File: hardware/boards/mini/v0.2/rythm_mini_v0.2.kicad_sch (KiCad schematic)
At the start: 76 parts, among them IC1 NAU88C22YG, IC2 IS42S32160F-6BLI, Q1 PMV37EN22, U1 W25Q128JVP, U2 LTV-217-G, U3 RythmMini, U4 STM32H750XBHx, Y1 Crystal_GND24

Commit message: place stm32h750 decoupling capacitors
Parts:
- added C2, C3: 2.2 uF <100 mΩ ESR, Capacitor_SMD:C_0402_1005Metric, symbol Device:C
- added C4: 1uF 600mΩ, Capacitor_SMD:C_0402_1005Metric, symbol Device:C_Small
- added C5: 100nF, Capacitor_SMD:C_0402_1005Metric, symbol Device:C_Small
- added C6: 1uF, Capacitor_SMD:C_0402_1005Metric, symbol Device:C_Small
- added R18: 10k, Resistor_SMD:R_0402_1005Metric, symbol Device:R
- R5: value 4.7k -> 10k; footprint Capacitor_SMD:C_0402_1005Metric -> Resistor_SMD:R_0402_1005Metric
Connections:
- net +3.3V: now also U4.E7 (PDR_ON), U4.F17 (VDD33_USB), U4.G17 (VDD50_USB), C4.1, C5.1, C6.1, R18.1
- net GND: now also C1.2, C2.2, C3.2, C4.2, C5.2, C6.2
- net at U4.A7 (VCAP): now also C3.1
- net at U4.D17 (VCAP): now also C2.1
- net BOOT0: now reaches U4.E8 (BOOT0)
- net BOOT0: now also R18.2
- net at U4.U11 (VCAP): now also C1.1
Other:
- note added: "TODO: should BOOT be high or low?"
- moved on the sheet: C1, C15, C30, C31, C32, C33, C48, C50, C51, C52, C54, C55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

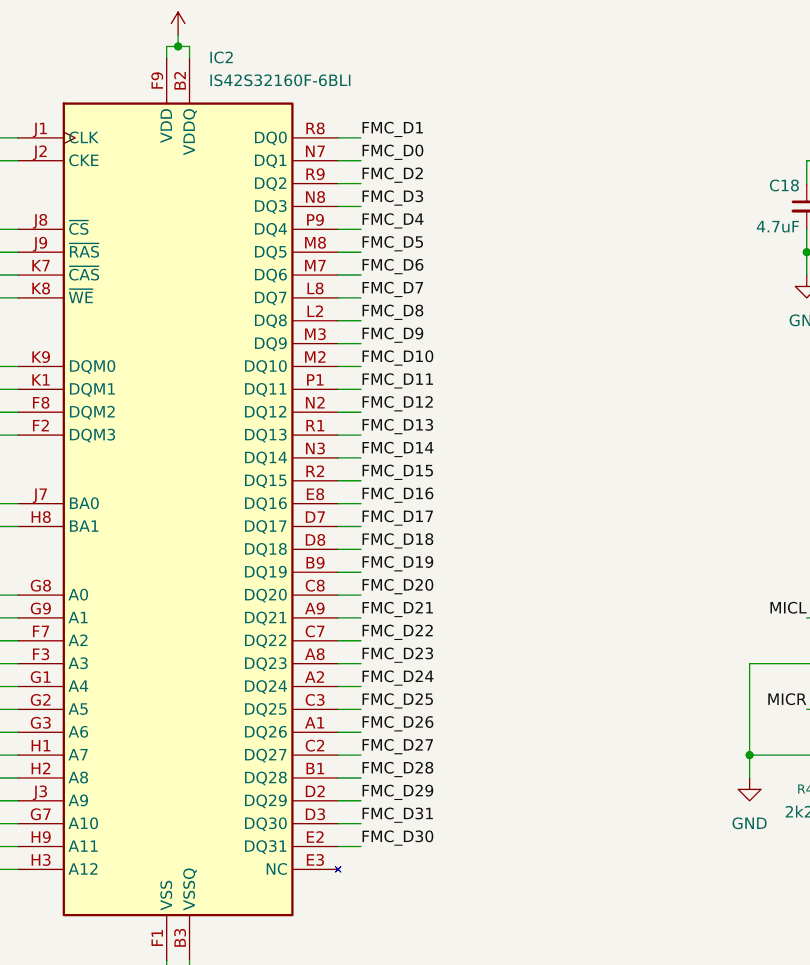
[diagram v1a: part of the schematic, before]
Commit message: mini: more SDRAM routing work
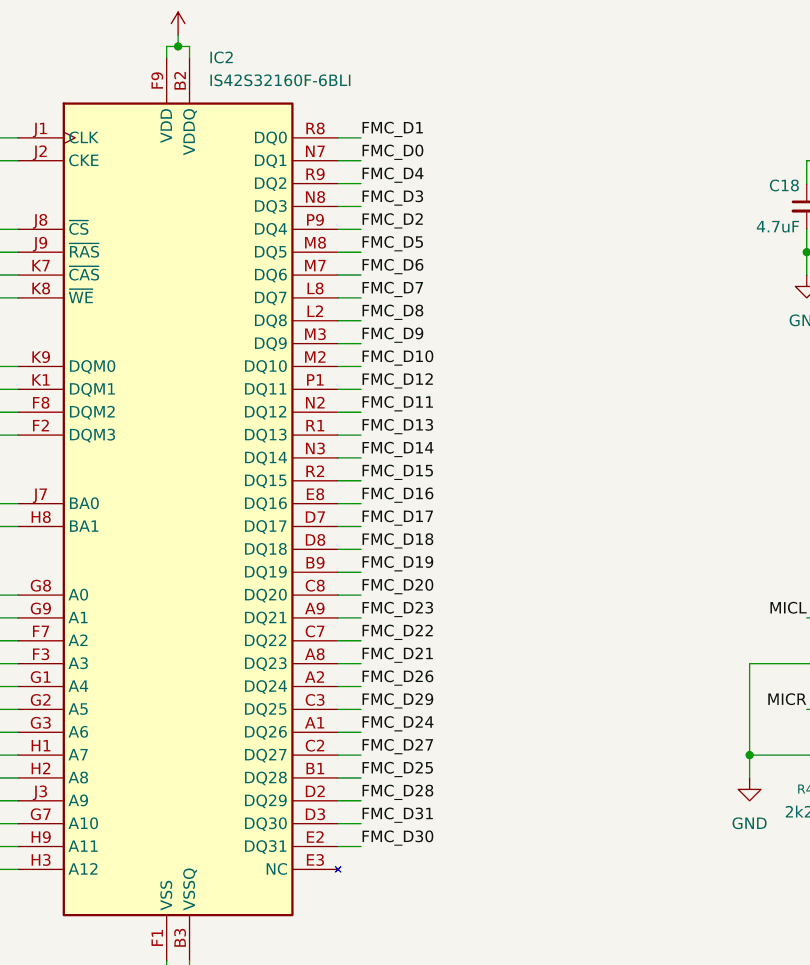
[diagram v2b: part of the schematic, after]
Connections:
- net FMC_D11: now also IC2.N2 (DQ12); no longer IC2.P1 (DQ11)
- net FMC_D12: now also IC2.P1 (DQ11); no longer IC2.N2 (DQ12)
- net FMC_D2: now also IC2.P9 (DQ4); no longer IC2.R9 (DQ2)
- net FMC_D21: now also IC2.A8 (DQ23); no longer IC2.A9 (DQ21)
- net FMC_D23: now also IC2.A9 (DQ21); no longer IC2.A8 (DQ23)
- net FMC_D24: now also IC2.A1 (DQ26); no longer IC2.A2 (DQ24)
- net FMC_D25: now also IC2.B1 (DQ28); no longer IC2.C3 (DQ25)
- net FMC_D26: now also IC2.A2 (DQ24); no longer IC2.A1 (DQ26)
- net FMC_D28: now also IC2.D2 (DQ29); no longer IC2.B1 (DQ28)
- net FMC_D29: now also IC2.C3 (DQ25); no longer IC2.D2 (DQ29)
- net FMC_D4: now also IC2.R9 (DQ2); no longer IC2.P9 (DQ4)
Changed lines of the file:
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@@
 	)
 	(label "FMC_D25"
-		(at 323.85 473.71 0)
+		(at 323.85 481.33 0)
 		(effects
 			(font
@@
 	)
 	(label "FMC_D11"
-		(at 323.85 438.15 0)
+		(at 323.85 440.69 0)
 		(effects
 			(font
@@
 	)
 	(label "FMC_D2"
-		(at 323.85 415.29 0)
+		(at 323.85 420.37 0)
 		(effects
 			(font
@@
 	)
 	(label "FMC_D26"
-		(at 323.85 476.25 0)
+		(at 323.85 471.17 0)
 		(effects
 			(font
@@
 	)
 	(label "FMC_D4"
-		(at 323.85 420.37 0)
+		(at 323.85 415.29 0)
 		(effects
 			(font
@@
 	)
 	(label "FMC_D24"
-		(at 323.85 471.17 0)
+		(at 323.85 476.25 0)
 		(effects
 			(font
@@
 	)
 	(label "FMC_D28"
-		(at 323.85 481.33 0)
+		(at 323.85 483.87 0)
 		(effects
 			(font
@@
 	)
 	(label "FMC_D12"
-		(at 323.85 440.69 0)
+		(at 323.85 438.15 0)
 		(effects
 			(font
@@
 	)
 	(label "FMC_D21"
-		(at 323.85 463.55 0)
+		(at 323.85 468.63 0)
 		(effects
 			(font
@@
 	)
 	(label "FMC_D23"
-		(at 323.85 468.63 0)
+		(at 323.85 463.55 0)
 		(effects
 			(font
@@
 	)
 	(label "FMC_D29"
-		(at 323.85 483.87 0)
-		(effects
-			(font
+		(at 323.85 473.71 0)
+		(effects
+			(font

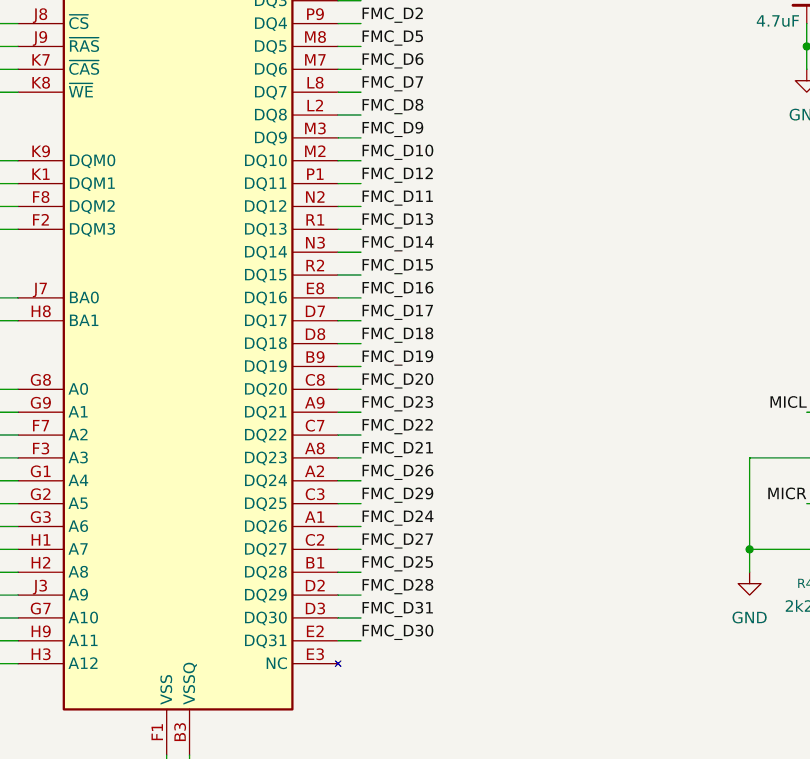
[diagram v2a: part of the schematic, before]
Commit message: second mini SDRAM routing attempt
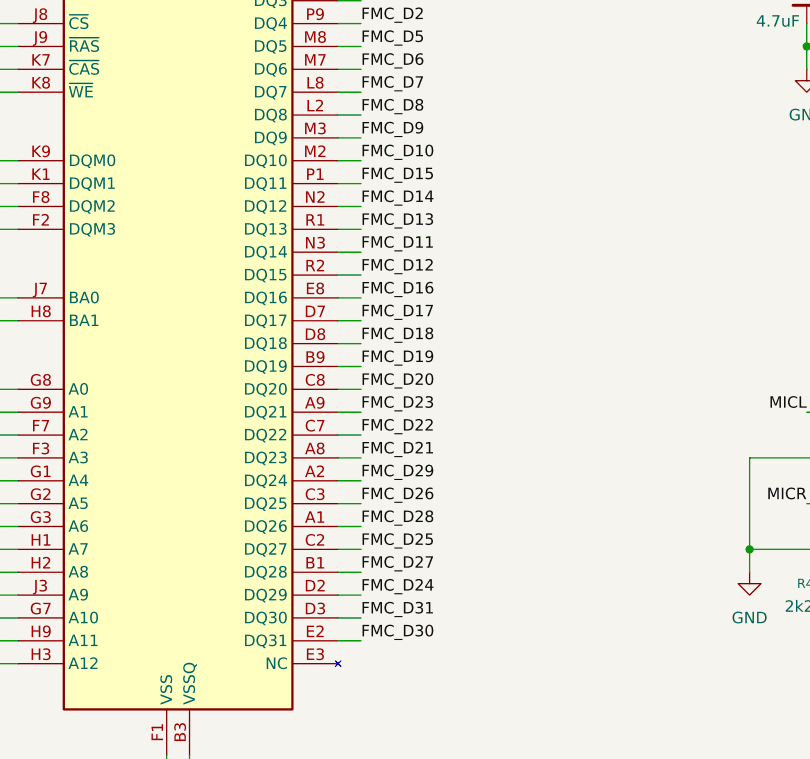
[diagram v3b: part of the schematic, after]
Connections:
- net FMC_D11: now also IC2.N3 (DQ14); no longer IC2.N2 (DQ12)
- net FMC_D12: now also IC2.R2 (DQ15); no longer IC2.P1 (DQ11)
- net FMC_D14: now also IC2.N2 (DQ12); no longer IC2.N3 (DQ14)
- net FMC_D15: now also IC2.P1 (DQ11); no longer IC2.R2 (DQ15)
- net FMC_D24: now also IC2.D2 (DQ29); no longer IC2.A1 (DQ26)
- net FMC_D25: now also IC2.C2 (DQ27); no longer IC2.B1 (DQ28)
- net FMC_D26: now also IC2.C3 (DQ25); no longer IC2.A2 (DQ24)
- net FMC_D27: now also IC2.B1 (DQ28); no longer IC2.C2 (DQ27)
- net FMC_D28: now also IC2.A1 (DQ26); no longer IC2.D2 (DQ29)
- net FMC_D29: now also IC2.A2 (DQ24); no longer IC2.C3 (DQ25)
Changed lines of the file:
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@@
 	)
 	(label "FMC_D25"
-		(at 323.85 481.33 0)
+		(at 323.85 478.79 0)
 		(effects
 			(font
@@
 	)
 	(label "FMC_D27"
-		(at 323.85 478.79 0)
+		(at 323.85 481.33 0)
 		(effects
 			(font
@@
 	)
 	(label "FMC_D11"
-		(at 323.85 440.69 0)
+		(at 323.85 445.77 0)
 		(effects
 			(font
@@
 	)
 	(label "FMC_D15"
-		(at 323.85 448.31 0)
+		(at 323.85 438.15 0)
 		(effects
 			(font
@@
 	)
 	(label "FMC_D26"
-		(at 323.85 471.17 0)
+		(at 323.85 473.71 0)
 		(effects
 			(font
@@
 	)
 	(label "FMC_D24"
-		(at 323.85 476.25 0)
+		(at 323.85 483.87 0)
 		(effects
 			(font
@@
 	)
 	(label "FMC_D14"
-		(at 323.85 445.77 0)
+		(at 323.85 440.69 0)
 		(effects
 			(font
@@
 	)
 	(label "FMC_D28"
-		(at 323.85 483.87 0)
+		(at 323.85 476.25 0)
 		(effects
 			(font
@@
 	)
 	(label "FMC_D12"
-		(at 323.85 438.15 0)
+		(at 323.85 448.31 0)
 		(effects
 			(font
@@
 	)
 	(label "FMC_D29"
-		(at 323.85 473.71 0)
-		(effects
-			(font
+		(at 323.85 471.17 0)
+		(effects
+			(font

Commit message: implement sine oscillator and example
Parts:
- added U5: MT48LC32M8A2TG, Package_SO:TSOP-II-54_22.2x10.16mm_P0.8mm, symbol Memory_RAM:MT48LC32M8A2TG
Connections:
- net FMC_D0: now also IC2.R8 (DQ0); no longer IC2.N7 (DQ1)
- net FMC_D1: now also IC2.N7 (DQ1); no longer IC2.R8 (DQ0)
- net FMC_D12: now also IC2.N2 (DQ12); no longer IC2.R2 (DQ15)
- net FMC_D13: now also IC2.P1 (DQ11); no longer IC2.R1 (DQ13)
- net FMC_D14: now also IC2.R1 (DQ13); no longer IC2.N2 (DQ12)
- net FMC_D15: now also IC2.R2 (DQ15); no longer IC2.P1 (DQ11)
- new net: U5.1 (VDD), U5.14 (VDD), U5.27 (VDD)
- new net: U5.12 (VSSQ), U5.46 (VSSQ), U5.52 (VSSQ), U5.6 (VSSQ)
- new net: U5.28 (VSS), U5.41 (VSS), U5.54 (VSS)
- new net: U5.3 (VDDQ), U5.43 (VDDQ), U5.49 (VDDQ), U5.9 (VDDQ)
